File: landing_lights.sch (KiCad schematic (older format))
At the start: 22 parts

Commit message: Continued syncing with original design.
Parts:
- removed C? (x2): C, ~, symbol C
- removed D? (x2): BI_LED, ~, symbol BI_LED
- removed F? (x4): FUSE, ~, symbol FUSE
- removed K?: CONN_3, symbol CONN_3
- removed Q? (x2): FET_N_GDS, symbol FET_N_GDS
- removed R? (x4): R, ~, symbol R
- removed U? (x2): 74LS74, ~, symbol 74LS74
- removed U? (x2): MIC5014, ~, symbol MIC5014
- added C14, C15: C, ~, symbol C
- added D6, D7: BI_LED, ~, symbol BI_LED
- added F24, F25, F26, F27: 1.1A 24V, ~, symbol FUSE
- added J22: JST-PA-3, ~, symbol CONN_3
- added Q3, Q4: FET_N_GDS, symbol FET_N_GDS
- added R25, R26, R27, R28: R, ~, symbol R
- added unit 2 of U10
- added unit 2 of U11
- added U12, U13: MIC5014, ~, symbol MIC5014
- J21: renamed from K?; value CONN_3 -> JST-PA-3; footprint (none) -> ~; Digikey (none) -> 455-2644-1-ND
- gave numbers to parts that had none: 2

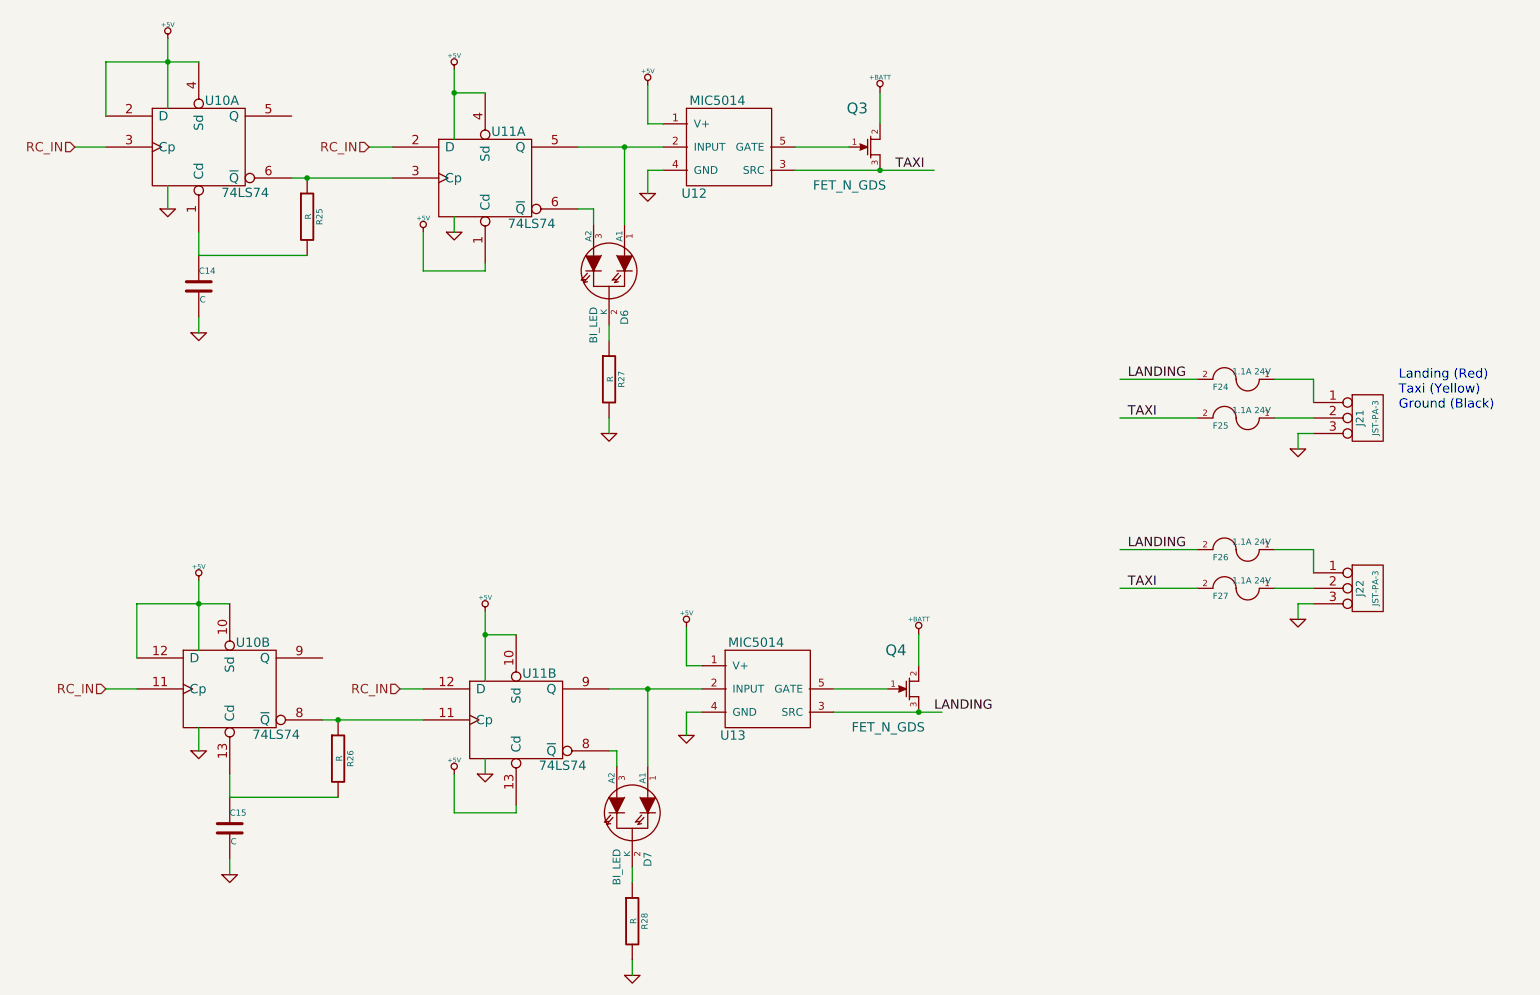
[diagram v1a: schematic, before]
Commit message: Finishing bom integration with schematic.
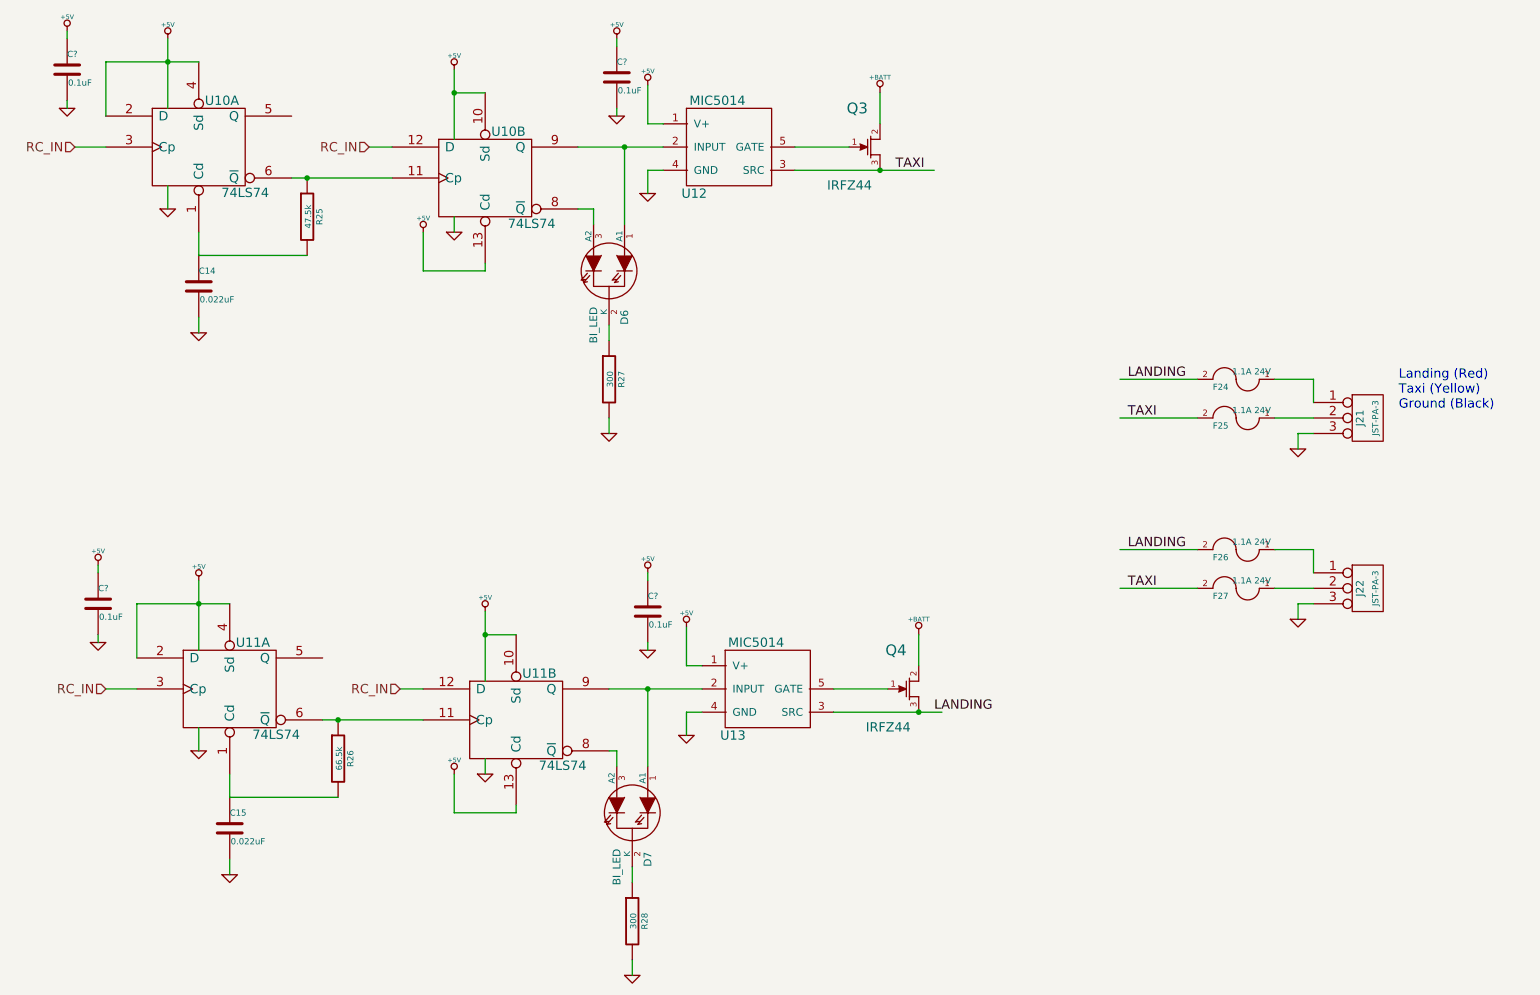
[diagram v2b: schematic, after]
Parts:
- added C? (x4): 0.1uF, SM0805, symbol C
- C14, C15: value C -> 0.022uF; Digikey (none) -> 490-8308-1-ND
- D6, D7: Digikey (none) -> VLMV3100-GS08CT-ND
- Q3, Q4: value FET_N_GDS -> IRFZ44; footprint (none) -> ~; Digikey (none) -> IRFZ44STRRPBFCT-ND
- R25: value R -> 47.5k; Digikey (none) -> P47.5KDACT-ND
- R26: value R -> 66.5k; Digikey (none) -> P66.5KDACT-ND
- R27, R28: value R -> 300; Digikey (none) -> P300CCT-ND
- U10, U11: Digikey (none) -> 296-1079-1-ND
- U10: renamed from U11; Digikey (none) -> 296-1079-1-ND
- U11: renamed from U10; Digikey (none) -> 296-1079-1-ND
- U12, U13: Digikey (none) -> 576-1233-1-ND
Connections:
- wire segments 72 -> 80
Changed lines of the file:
@@
 LIBS:p_samtec
 LIBS:w_transistor
+LIBS:w_analog
 LIBS:distro-cache
 EELAYER 27 0
@@
 Sheet 6 9
 Title ""
-Date "21 aug 2015"
+Date "22 aug 2015"
 Rev ""
 Comp ""
@@
 $EndDescr
 $Comp
-L 74LS74 U10
-U 2 1 55D6B09C
+L 74LS74 U11
+U 1 1 55D6B09C
 P 2100 5150
-F 0 "U10" H 2250 5450 60  0000 C CNN
+F 0 "U11" H 2250 5450 60  0000 C CNN
 F 1 "74LS74" H 2400 4855 60  0000 C CNN
 F 2 "~" H 2100 5150 60  0000 C CNN
 F 3 "~" H 2100 5150 60  0000 C CNN
-	2    2100 5150
+F 4 "296-1079-1-ND" H 2100 5150 60  0001 C CNN "Digikey"
+	1    2100 5150
 	1    0    0    -1
 $EndComp
@@
 F 2 "~" H 3950 5350 60  0000 C CNN
 F 3 "~" H 3950 5350 60  0000 C CNN
+F 4 "296-1079-1-ND" H 3950 5350 60  0001 C CNN "Digikey"
 	2    3950 5350
 	1    0    0    -1
@@
 P 2100 6050
 F 0 "C15" H 2100 6150 40  0000 L CNN
-F 1 "C" H 2106 5965 40  0000 L CNN
+F 1 "0.022uF" H 2106 5965 40  0000 L CNN
 F 2 "~" H 2138 5900 30  0000 C CNN
 F 3 "~" H 2100 6050 60  0000 C CNN
+F 4 "490-8308-1-ND" H 2100 6050 60  0001 C CNN "Digikey"
 	1    2100 6050
 	1    0    0    -1
@@
 P 2800 5600
 F 0 "R26" V 2880 5600 40  0000 C CNN
-F 1 "R" V 2807 5601 40  0000 C CNN
+F 1 "66.5k" V 2807 5601 40  0000 C CNN
 F 2 "~" V 2730 5600 30  0000 C CNN
 F 3 "~" H 2800 5600 30  0000 C CNN
+F 4 "P66.5KDACT-ND" V 2800 5600 60  0001 C CNN "Digikey"
 	1    2800 5600
 	1    0    0    -1
@@
 F 2 "~" H 5450 5050 60  0000 C CNN
 F 3 "~" H 5450 5050 60  0000 C CNN
+F 4 "576-1233-1-ND" H 5600 5150 60  0001 C CNN "Digikey"
 	1    5600 5150
 	1    0    0    -1
@@
 P 6500 5150
 F 0 "Q4" H 6403 5400 70  0000 C CNN
-F 1 "FET_N_GDS" H 6353 4903 60  0000 C CNN
-F 2 "" H 6500 5150 60  0000 C CNN
-F 3 "" H 6500 5150 60  0000 C CNN
+F 1 "IRFZ44" H 6353 4903 60  0000 C CNN
+F 2 "~" H 6500 5150 60  0000 C CNN
+F 3 "~" H 6500 5150 60  0000 C CNN
+F 4 "IRFZ44STRRPBFCT-ND" H 6500 5150 60  0001 C CNN "Digikey"
 	1    6500 5150
 	1    0    0    -1
@@
 F 2 "~" H 1900 1650 60  0000 C CNN
 F 3 "~" H 1900 1650 60  0000 C CNN
+F 4 "296-1079-1-ND" H 1900 1650 60  0001 C CNN "Digikey"
 	1    1900 1650
 	1    0    0    -1
 $EndComp
 $Comp
-L 74LS74 U11
-U 1 1 55CD3F39
+L 74LS74 U10
+U 2 1 55CD3F39
 P 3750 1850
-F 0 "U11" H 3900 2150 60  0000 C CNN
+F 0 "U10" H 3900 2150 60  0000 C CNN
 F 1 "74LS74" H 4050 1555 60  0000 C CNN
 F 2 "~" H 3750 1850 60  0000 C CNN
 F 3 "~" H 3750 1850 60  0000 C CNN
-	1    3750 1850
+F 4 "296-1079-1-ND" H 3750 1850 60  0001 C CNN "Digikey"
+	2    3750 1850
 	1    0    0    -1
 $EndComp
@@
 P 1900 2550
 F 0 "C14" H 1900 2650 40  0000 L CNN
-F 1 "C" H 1906 2465 40  0000 L CNN
+F 1 "0.022uF" H 1906 2465 40  0000 L CNN
 F 2 "~" H 1938 2400 30  0000 C CNN
 F 3 "~" H 1900 2550 60  0000 C CNN
+F 4 "490-8308-1-ND" H 1900 2550 60  0001 C CNN "Digikey"
 	1    1900 2550
 	1    0    0    -1
@@
 P 2600 2100
 F 0 "R25" V 2680 2100 40  0000 C CNN
-F 1 "R" V 2607 2101 40  0000 C CNN
+F 1 "47.5k" V 2607 2101 40  0000 C CNN
 F 2 "~" V 2530 2100 30  0000 C CNN
 F 3 "~" H 2600 2100 30  0000 C CNN
+F 4 "P47.5KDACT-ND" V 2600 2100 60  0001 C CNN "Digikey"
 	1    2600 2100
 	1    0    0    -1
@@
 F 2 "~" H 5200 1550 60  0000 C CNN
 F 3 "~" H 5200 1550 60  0000 C CNN
+F 4 "576-1233-1-ND" H 5350 1650 60  0001 C CNN "Digikey"
 	1    5350 1650
 	1    0    0    -1
@@
 P 6250 1650
 F 0 "Q3" H 6153 1900 70  0000 C CNN
-F 1 "FET_N_GDS" H 6103 1403 60  0000 C CNN
-F 2 "" H 6250 1650 60  0000 C CNN
-F 3 "" H 6250 1650 60  0000 C CNN
+F 1 "IRFZ44" H 6103 1403 60  0000 C CNN
+F 2 "~" H 6250 1650 60  0000 C CNN
+F 3 "~" H 6250 1650 60  0000 C CNN
+F 4 "IRFZ44STRRPBFCT-ND" H 6250 1650 60  0001 C CNN "Digikey"
 	1    6250 1650
 	1    0    0    -1
@@
 F 2 "~" H 4700 5950 60  0000 C CNN
 F 3 "~" H 4700 5950 60  0000 C CNN
+F 4 "VLMV3100-GS08CT-ND" H 4700 5950 60  0001 C CNN "Digikey"
 	1    4700 5950
 	0    1    1    0
@@
 F 2 "~" H 4550 2450 60  0000 C CNN
 F 3 "~" H 4550 2450 60  0000 C CNN
+F 4 "VLMV3100-GS08CT-ND" H 4550 2450 60  0001 C CNN "Digikey"
 	1    4550 2450
 	0    1    1    0
@@
 P 4550 3150
 F 0 "R27" V 4630 3150 40  0000 C CNN
-F 1 "R" V 4557 3151 40  0000 C CNN
+F 1 "300" V 4557 3151 40  0000 C CNN
 F 2 "~" V 4480 3150 30  0000 C CNN
 F 3 "~" H 4550 3150 30  0000 C CNN
+F 4 "P300CCT-ND" V 4550 3150 60  0001 C CNN "Digikey"
 	1    4550 3150
 	1    0    0    -1
@@
 P 4700 6650
 F 0 "R28" V 4780 6650 40  0000 C CNN
-F 1 "R" V 4707 6651 40  0000 C CNN
+F 1 "300" V 4707 6651 40  0000 C CNN
 F 2 "~" V 4630 6650 30  0000 C CNN
 F 3 "~" H 4700 6650 30  0000 C CNN
+F 4 "P300CCT-ND" V 4700 6650 60  0001 C CNN "Digikey"
 	1    4700 6650
 	1    0    0    -1
@@
 	1    0    0    -1
 $EndComp
+$Comp
+L C C?
+U 1 1 55D805D4
+P 1050 1150
+F 0 "C?" H 1050 1250 40  0000 L CNN
+F 1 "0.1uF" H 1056 1065 40  0000 L CNN
+F 2 "SM0805" H 1088 1000 30  0001 C CNN
+F 3 "~" H 1050 1150 60  0000 C CNN
+F 4 "399-11163-1-ND" H 1050 1150 60  0001 C CNN "Digikey"
+	1    1050 1150
+	1    0    0    -1
+$EndComp
+$Comp
+L +5V #PWR?
+U 1 1 55D805DA
+P 1050 900
+F 0 "#PWR?" H 1050 990 20  0001 C CNN
+F 1 "+5V" H 1050 990 30  0000 C CNN
+F 2 "" H 1050 900 60  0000 C CNN
+F 3 "" H 1050 900 60  0000 C CNN
+	1    1050 900
+	1    0    0    -1
+$EndComp
+$Comp
+L GND #PWR?
+U 1 1 55D805E0
+P 1050 1400
+F 0 "#PWR?" H 1050 1400 30  0001 C CNN
+F 1 "GND" H 1050 1330 30  0001 C CNN
+F 2 "" H 1050 1400 60  0000 C CNN
+F 3 "" H 1050 1400 60  0000 C CNN
+	1    1050 1400
+	1    0    0    -1
+$EndComp
+Wire Wire Line
+	1050 1400 1050 1350
+Wire Wire Line
+	1050 950  1050 900
+$Comp
+L C C?
+U 1 1 55D805E9
+P 4600 1200
+F 0 "C?" H 4600 1300 40  0000 L CNN
+F 1 "0.1uF" H 4606 1115 40  0000 L CNN
+F 2 "SM0805" H 4638 1050 30  0001 C CNN
+F 3 "~" H 4600 1200 60  0000 C CNN
+F 4 "399-11163-1-ND" H 4600 1200 60  0001 C CNN "Digikey"
+	1    4600 1200
+	1    0    0    -1
+$EndComp
+$Comp
+L +5V #PWR?
+U 1 1 55D805EF
+P 4600 950
+F 0 "#PWR?" H 4600 1040 20  0001 C CNN
+F 1 "+5V" H 4600 1040 30  0000 C CNN
+F 2 "" H 4600 950 60  0000 C CNN
+F 3 "" H 4600 950 60  0000 C CNN
+	1    4600 950
+	1    0    0    -1
+$EndComp
+$Comp
+L GND #PWR?
+U 1 1 55D805F5
+P 4600 1450
+F 0 "#PWR?" H 4600 1450 30  0001 C CNN
+F 1 "GND" H 4600 1380 30  0001 C CNN
+F 2 "" H 4600 1450 60  0000 C CNN
+F 3 "" H 4600 1450 60  0000 C CNN
+	1    4600 1450
+	1    0    0    -1
+$EndComp
+Wire Wire Line
+	4600 1450 4600 1400
+Wire Wire Line
+	4600 1000 4600 950
+$Comp
+L C C?
+U 1 1 55D80613
+P 1250 4600
+F 0 "C?" H 1250 4700 40  0000 L CNN
+F 1 "0.1uF" H 1256 4515 40  0000 L CNN
+F 2 "SM0805" H 1288 4450 30  0001 C CNN
+F 3 "~" H 1250 4600 60  0000 C CNN
+F 4 "399-11163-1-ND" H 1250 4600 60  0001 C CNN "Digikey"
+	1    1250 4600
+	1    0    0    -1
+$EndComp
+$Comp
+L +5V #PWR?
+U 1 1 55D80619
+P 1250 4350
+F 0 "#PWR?" H 1250 4440 20  0001 C CNN
+F 1 "+5V" H 1250 4440 30  0000 C CNN
+F 2 "" H 1250 4350 60  0000 C CNN
+F 3 "" H 1250 4350 60  0000 C CNN
+	1    1250 4350
+	1    0    0    -1
+$EndComp
+$Comp
+L GND #PWR?
+U 1 1 55D8061F
+P 1250 4850
+F 0 "#PWR?" H 1250 4850 30  0001 C CNN
+F 1 "GND" H 1250 4780 30  0001 C CNN
+F 2 "" H 1250 4850 60  0000 C CNN
+F 3 "" H 1250 4850 60  0000 C CNN
+	1    1250 4850
+	1    0    0    -1
+$EndComp
+Wire Wire Line
+	1250 4850 1250 4800
+Wire Wire Line
+	1250 4400 1250 4350
+$Comp
+L C C?
+U 1 1 55D8081D
+P 4800 4650
+F 0 "C?" H 4800 4750 40  0000 L CNN
+F 1 "0.1uF" H 4806 4565 40  0000 L CNN
+F 2 "SM0805" H 4838 4500 30  0001 C CNN
+F 3 "~" H 4800 4650 60  0000 C CNN
+F 4 "399-11163-1-ND" H 4800 4650 60  0001 C CNN "Digikey"
+	1    4800 4650
+	1    0    0    -1
+$EndComp
+$Comp
+L +5V #PWR?
+U 1 1 55D80823
+P 4800 4400
+F 0 "#PWR?" H 4800 4490 20  0001 C CNN
+F 1 "+5V" H 4800 4490 30  0000 C CNN
+F 2 "" H 4800 4400 60  0000 C CNN
+F 3 "" H 4800 4400 60  0000 C CNN
+	1    4800 4400
+	1    0    0    -1
+$EndComp
+$Comp
+L GND #PWR?
+U 1 1 55D80829
+P 4800 4900
+F 0 "#PWR?" H 4800 4900 30  0001 C CNN
+F 1 "GND" H 4800 4830 30  0001 C CNN
+F 2 "" H 4800 4900 60  0000 C CNN
+F 3 "" H 4800 4900 60  0000 C CNN
+	1    4800 4900
+	1    0    0    -1
+$EndComp
+Wire Wire Line
+	4800 4900 4800 4850
+Wire Wire Line
+	4800 4450 4800 4400
 $EndSCHEMATC
